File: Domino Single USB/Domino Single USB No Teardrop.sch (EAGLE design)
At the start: 9 parts, among them J1 MH4-1

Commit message: Changed copyright
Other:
- note added: "The Domino Team may make changes to specifications and product"
- note added: "© 2014, The Domino Team All rights reserved."
- note removed: "Michel Stempin may make changes to specifications and product"
- note removed: "© 2014, Michel Stempin All rights reserved."
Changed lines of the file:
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@@
 <text x="302.26" y="12.7" size="0.8128" layer="94">Reference designs are provided "AS IS" and "WITH ALL FAULTS".</text>
 <text x="302.26" y="10.16" size="0.8128" layer="94">regarding this product, including but not limited to, any implied warranties of</text>
-<text x="302.26" y="6.35" size="0.8128" layer="94">Michel Stempin may make changes to specifications and product </text>
+<text x="302.26" y="6.35" size="0.8128" layer="94">The Domino Team may make changes to specifications and product </text>
 <text x="302.26" y="11.43" size="0.8128" layer="94">Global Marine Networks disclaims all other warranties express or implied, </text>
 <text x="302.26" y="8.89" size="0.8128" layer="94">merchantibility or fitness for any particular application.</text>
@@
 <text x="256.54" y="7.62" size="1.778" layer="94" align="center">Domino
 Qi</text>
-<text x="345.44" y="20.32" size="1.27" layer="94">© 2014, Michel Stempin
+<text x="345.44" y="20.32" size="1.27" layer="94">© 2014, The Domino Team
 All rights reserved.</text>
 <text x="379.222" y="5.334" size="1.778" layer="94">&gt;REV</text>

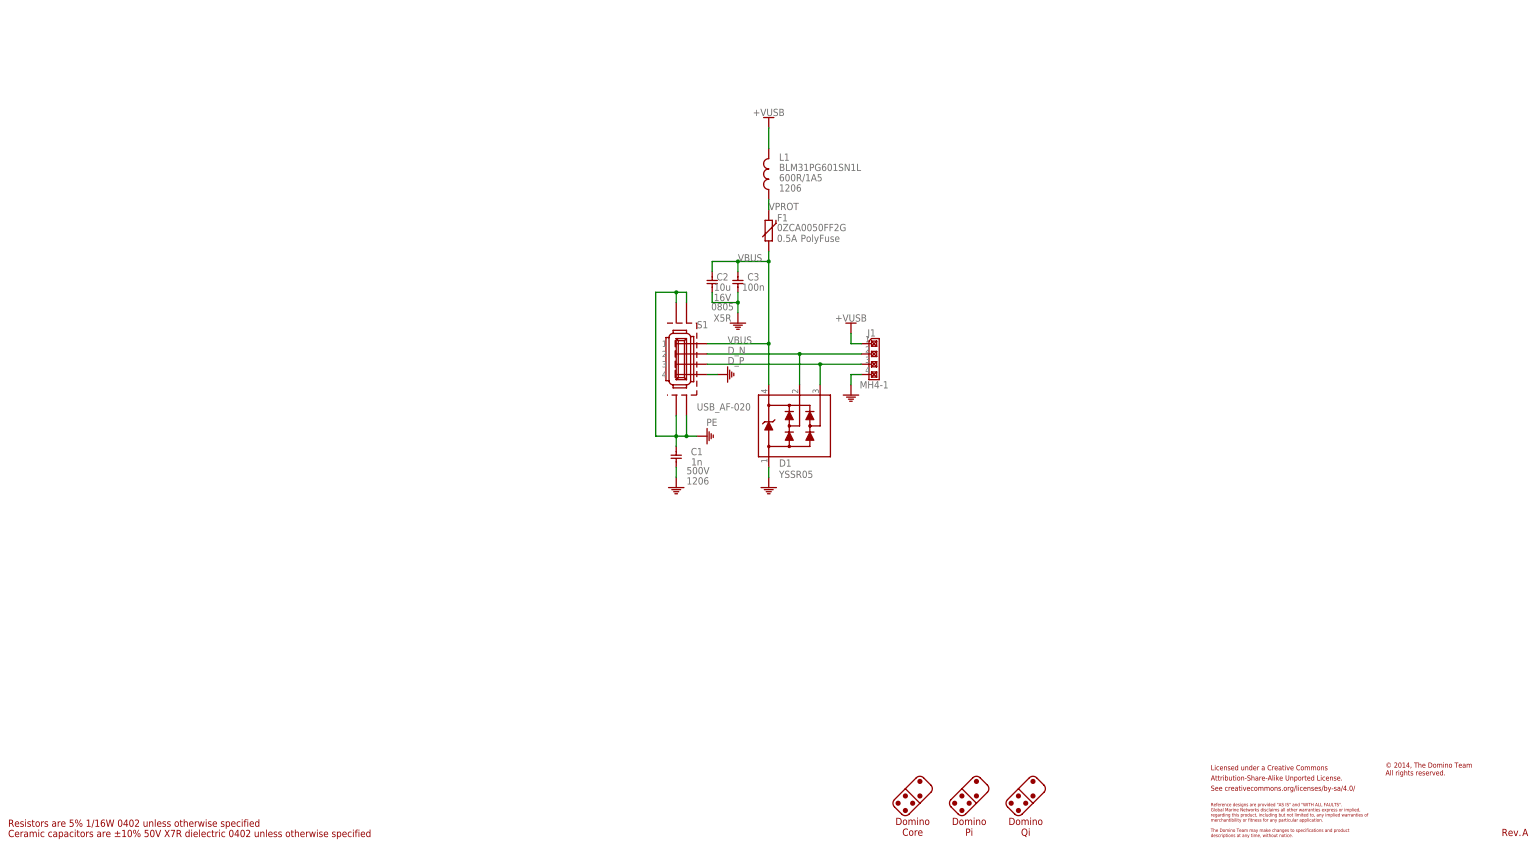
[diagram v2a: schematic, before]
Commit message: Domino Single USB tile Revision B
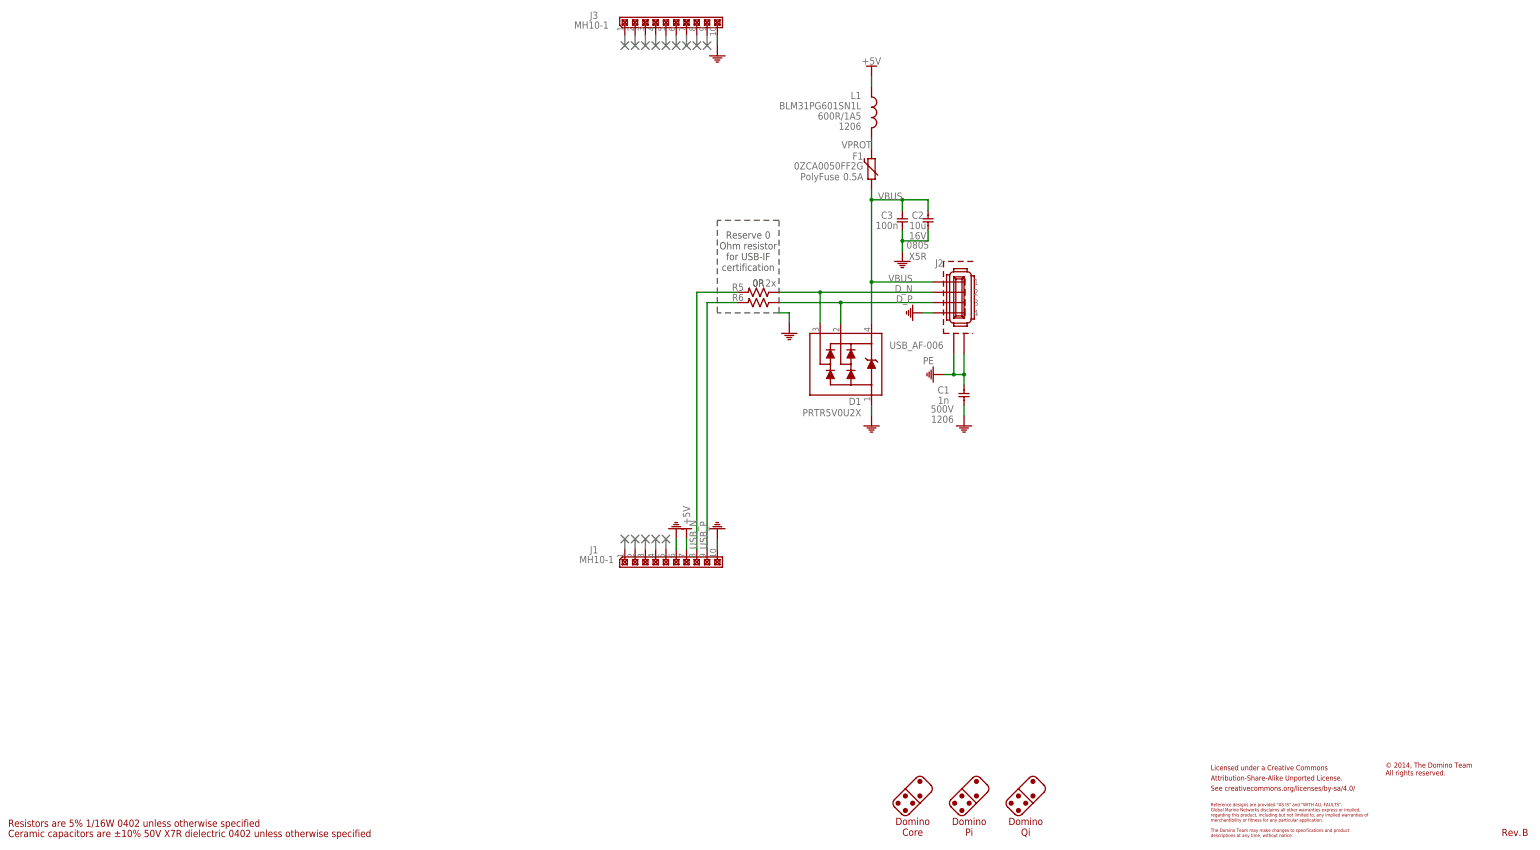
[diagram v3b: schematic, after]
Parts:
- removed S1: USB_AF-020, Domino:USB_AF-020
- added J2: USB_AF-006, Domino:USB_AF-006
- added J3: MH10-1, Domino:MH10-1
- added R5, R6: 0R, Domino:RES_0402
- D1: value YSSR05 -> PRTR5V0U2X; device Domino:YSSR05 -> Domino:PRTR5V0U2X; PARTNO YSSR05 -> PRTR5V0U2X
- J1: value MH4-1 -> MH10-1; device Domino:MH4-1 -> Domino:MH10-1; PARTNO MH4-1-0.1 -> MH10-1-0.1
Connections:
- removed net +VUSB: J1.1, L1.1
- new net +5V: J1.7, L1.1
- new net USB_N: J1.8, R5.2
- new net USB_P: J1.9, R6.2
- net D_N: now also D1.P$3, J2.2, R5.1; no longer D1.P$2, J1.2, S1.2
- net D_P: now also D1.P$2, J2.3, R6.1; no longer D1.P$3, J1.3, S1.3
- net GND: now also J1.10, J1.6, J2.4, J3.10; no longer J1.4, S1.4
- net PE: now also J2.G@1, J2.G@2; no longer S1.G@1, S1.G@2, S1.G@3, S1.G@4
- net VBUS: now also J2.1; no longer S1.1
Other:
- note added: "2x"
- note added: "Reserve 0 Ohm resistor for USB-IF certification"
- moved on the sheet: C1, C2, C3, D1, F1, L1

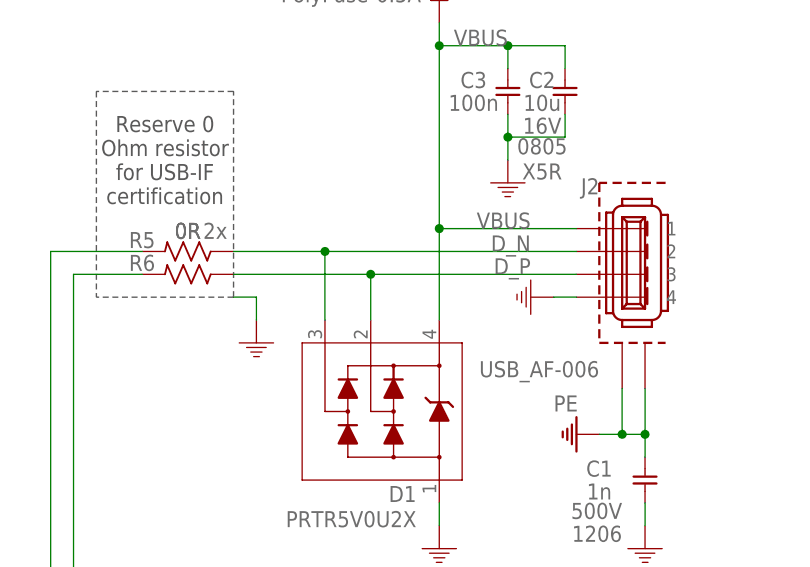
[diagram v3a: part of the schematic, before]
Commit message: Re-routed Single USB tile to remove vias on USB traces
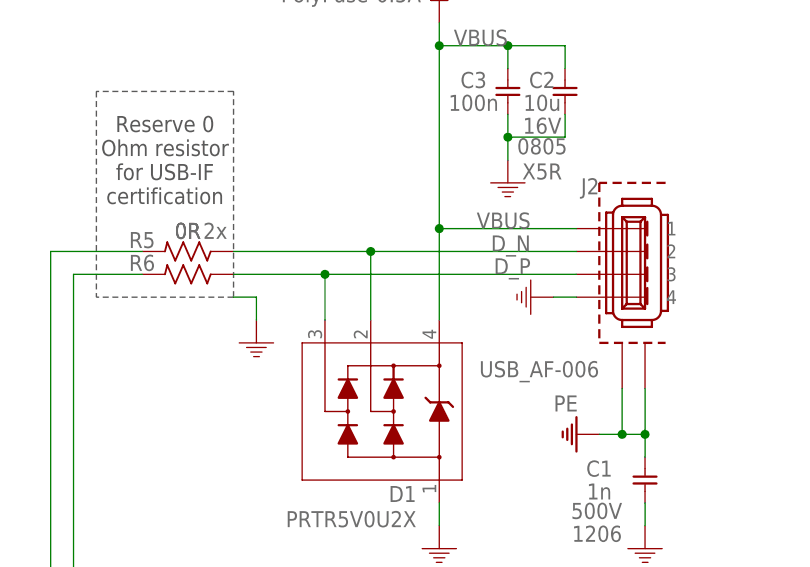
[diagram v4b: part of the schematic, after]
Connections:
- net D_N: now also D1.P$2; no longer D1.P$3
- net D_P: now also D1.P$3; no longer D1.P$2
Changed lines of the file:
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@@
 <net name="D_N" class="1">
 <segment>
-<wire x1="233.68" y1="139.7" x2="205.74" y2="139.7" width="0.1524" layer="91"/>
+<wire x1="233.68" y1="139.7" x2="210.82" y2="139.7" width="0.1524" layer="91"/>
 <label x="228.6" y="139.7" size="1.778" layer="95" rot="MR0"/>
 <pinref part="J2" gate="G$1" pin="2"/>
 <pinref part="R5" gate="G$1" pin="1"/>
-<pinref part="D1" gate="G$1" pin="P$3"/>
-<wire x1="205.74" y1="139.7" x2="195.58" y2="139.7" width="0.1524" layer="91"/>
-<wire x1="205.74" y1="132.08" x2="205.74" y2="139.7" width="0.1524" layer="91"/>
-<junction x="205.74" y="139.7"/>
+<pinref part="D1" gate="G$1" pin="P$2"/>
+<wire x1="210.82" y1="139.7" x2="195.58" y2="139.7" width="0.1524" layer="91"/>
+<wire x1="210.82" y1="132.08" x2="210.82" y2="139.7" width="0.1524" layer="91"/>
+<junction x="210.82" y="139.7"/>
 </segment>
 </net>
 <net name="D_P" class="1">
 <segment>
-<wire x1="195.58" y1="137.16" x2="210.82" y2="137.16" width="0.1524" layer="91"/>
 <label x="228.6" y="137.16" size="1.778" layer="95" rot="MR0"/>
 <pinref part="J2" gate="G$1" pin="3"/>
 <pinref part="R6" gate="G$1" pin="1"/>
-<pinref part="D1" gate="G$1" pin="P$2"/>
-<wire x1="210.82" y1="137.16" x2="233.68" y2="137.16" width="0.1524" layer="91"/>
-<wire x1="210.82" y1="132.08" x2="210.82" y2="137.16" width="0.1524" layer="91"/>
-<junction x="210.82" y="137.16"/>
+<wire x1="195.58" y1="137.16" x2="205.74" y2="137.16" width="0.1524" layer="91"/>
+<pinref part="D1" gate="G$1" pin="P$3"/>
+<wire x1="205.74" y1="137.16" x2="233.68" y2="137.16" width="0.1524" layer="91"/>
+<wire x1="205.74" y1="132.08" x2="205.74" y2="137.16" width="0.1524" layer="91"/>
+<junction x="205.74" y="137.16"/>
 </segment>
 </net>

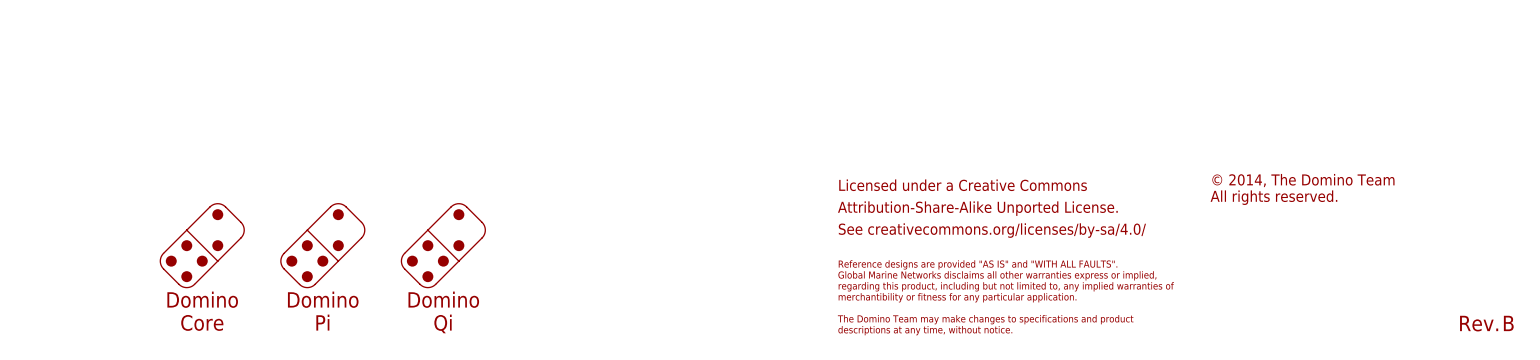
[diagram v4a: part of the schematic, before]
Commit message: Domino Single USB Rev. C: changed Logos
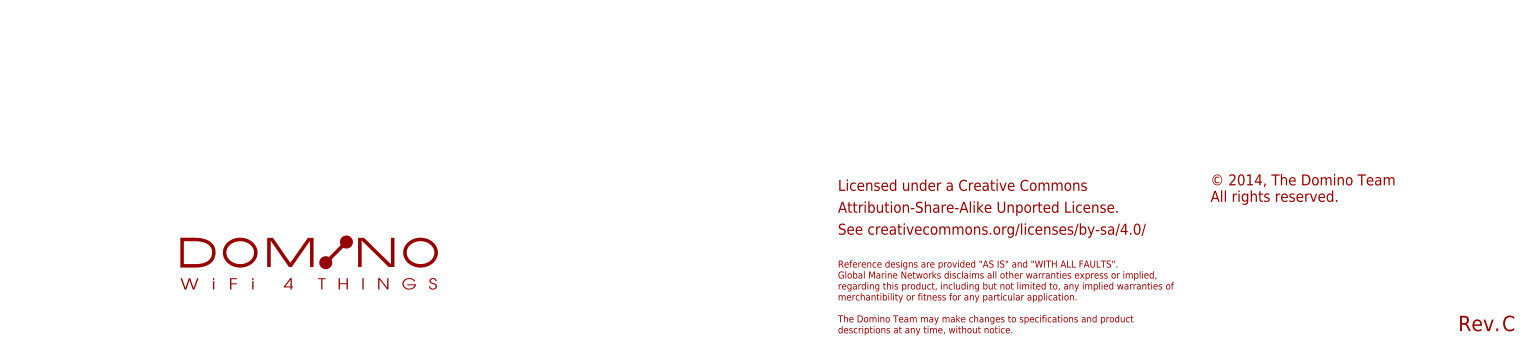
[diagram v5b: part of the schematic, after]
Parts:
- added U$7: DOMINO_LOGO, Domino:DOMINO_LOGO
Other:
- note removed: "Domino Core"
- note removed: "Domino Pi"
- note removed: "Domino Qi"
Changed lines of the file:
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@@
 <layer number="54" name="bGND_GNDA" color="1" fill="9" visible="no" active="no"/>
 <layer number="56" name="wert" color="7" fill="1" visible="no" active="no"/>
+<layer number="90" name="Modules" color="5" fill="1" visible="yes" active="yes"/>
 <layer number="91" name="Nets" color="2" fill="1" visible="yes" active="yes"/>
 <layer number="92" name="Busses" color="1" fill="1" visible="yes" active="yes"/>
@@
 <layer number="143" name="mvRestrict" color="7" fill="1" visible="no" active="no"/>
 <layer number="144" name="Drill_legend" color="7" fill="1" visible="yes" active="yes"/>
+<layer number="145" name="DrillLegend_01-16" color="2" fill="9" visible="yes" active="yes"/>
+<layer number="146" name="DrillLegend_01-20" color="3" fill="9" visible="yes" active="yes"/>
 <layer number="147" name="Measures_X8" color="7" fill="1" visible="yes" active="yes"/>
 <layer number="148" name="mDocument" color="7" fill="1" visible="no" active="no"/>
 <layer number="149" name="mReference" color="7" fill="1" visible="no" active="no"/>
+<layer number="150" name="Pinout" color="7" fill="1" visible="yes" active="yes"/>
 <layer number="151" name="HeatSink" color="7" fill="1" visible="yes" active="yes"/>
 <layer number="152" name="mbDocu" color="7" fill="1" visible="no" active="no"/>
@@
 <attribute name="DATABASE" value="./../Common/BOM/Domino_DB.txt"/>
 <attribute name="DRAWN" value="M.STEMPIN"/>
-<attribute name="REV" value="B"/>
+<attribute name="REV" value="C"/>
 </attributes>
 <variantdefs>
@@
 <part name="PORT13" library="Domino" deviceset="NC" device=""/>
 <part name="PORT14" library="Domino" deviceset="NC" device=""/>
+<part name="U$7" library="Domino" deviceset="DOMINO_LOGO" device=""/>
 </parts>
 <sheets>
@@
 <text x="302.26" y="8.89" size="0.8128" layer="94">merchantibility or fitness for any particular application.</text>
 <text x="302.26" y="5.08" size="0.8128" layer="94">descriptions at any time, without notice.</text>
-<wire x1="238.079875" y1="14.341975" x2="240.77395" y2="17.036053125" width="0.1016" layer="94"/>
-<wire x1="240.77395" y1="17.036053125" x2="243.468028125" y2="19.730128125" width="0.1016" layer="94"/>
-<wire x1="243.468028125" y1="19.730128125" x2="245.264078125" y2="19.730128125" width="0.1016" layer="94" curve="-90"/>
-<wire x1="245.264078125" y1="19.730128125" x2="247.060128125" y2="17.934078125" width="0.1016" layer="94"/>
-<wire x1="247.060128125" y1="17.934078125" x2="247.060128125" y2="16.138028125" width="0.1016" layer="94" curve="-90"/>
-<wire x1="247.060128125" y1="16.138028125" x2="244.366053125" y2="13.44395" width="0.1016" layer="94"/>
-<wire x1="244.366053125" y1="13.44395" x2="241.671975" y2="10.749875" width="0.1016" layer="94"/>
-<wire x1="241.671975" y1="10.749875" x2="239.875925" y2="10.749875" width="0.1016" layer="94" curve="-90"/>
-<wire x1="239.875925" y1="10.749875" x2="238.079875" y2="12.545925" width="0.1016" layer="94"/>
-<wire x1="238.079875" y1="12.545925" x2="238.079875" y2="14.341975" width="0.1016" layer="94" curve="-90"/>
-<wire x1="240.77395" y1="17.036053125" x2="244.366053125" y2="13.44395" width="0.1016" layer="94"/>
-<circle x="238.9779" y="13.44395" radius="0.635" width="0" layer="94"/>
-<circle x="240.77395" y="15.240003125" radius="0.635" width="0" layer="94"/>
-<circle x="240.77395" y="11.6479" radius="0.635" width="0" layer="94"/>
-<circle x="242.57" y="13.44395" radius="0.635" width="0" layer="94"/>
-<circle x="244.366053125" y="15.24" radius="0.635" width="0" layer="94"/>
-<circle x="244.366053125" y="18.832103125" radius="0.635" width="0" layer="94"/>
-<wire x1="224.109875" y1="14.341975" x2="226.80395" y2="17.036053125" width="0.1016" layer="94"/>
-<wire x1="226.80395" y1="17.036053125" x2="229.498028125" y2="19.730128125" width="0.1016" layer="94"/>
-<wire x1="229.498028125" y1="19.730128125" x2="231.294078125" y2="19.730128125" width="0.1016" layer="94" curve="-90"/>
-<wire x1="231.294078125" y1="19.730128125" x2="233.090128125" y2="17.934078125" width="0.1016" layer="94"/>
-<wire x1="233.090128125" y1="17.934078125" x2="233.090128125" y2="16.138028125" width="0.1016" layer="94" curve="-90"/>
-<wire x1="233.090128125" y1="16.138028125" x2="230.396053125" y2="13.44395" width="0.1016" layer="94"/>
-<wire x1="230.396053125" y1="13.44395" x2="227.701975" y2="10.749875" width="0.1016" layer="94"/>
-<wire x1="227.701975" y1="10.749875" x2="225.905925" y2="10.749875" width="0.1016" layer="94" curve="-90"/>
-<wire x1="225.905925" y1="10.749875" x2="224.109875" y2="12.545925" width="0.1016" layer="94"/>
-<wire x1="224.109875" y1="12.545925" x2="224.109875" y2="14.341975" width="0.1016" layer="94" curve="-90"/>
-<wire x1="226.80395" y1="17.036053125" x2="230.396053125" y2="13.44395" width="0.1016" layer="94"/>
-<circle x="225.0079" y="13.44395" radius="0.635" width="0" layer="94"/>
-<circle x="226.80395" y="15.240003125" radius="0.635" width="0" layer="94"/>
-<circle x="226.80395" y="11.6479" radius="0.635" width="0" layer="94"/>
-<circle x="228.6" y="13.44395" radius="0.635" width="0" layer="94"/>
-<circle x="230.396053125" y="15.24" radius="0.635" width="0" layer="94"/>
-<circle x="230.396053125" y="18.832103125" radius="0.635" width="0" layer="94"/>
-<wire x1="252.049875" y1="14.341975" x2="254.74395" y2="17.036053125" width="0.1016" layer="94"/>
-<wire x1="254.74395" y1="17.036053125" x2="257.438028125" y2="19.730128125" width="0.1016" layer="94"/>
-<wire x1="257.438028125" y1="19.730128125" x2="259.234078125" y2="19.730128125" width="0.1016" layer="94" curve="-90"/>
-<wire x1="259.234078125" y1="19.730128125" x2="261.030128125" y2="17.934078125" width="0.1016" layer="94"/>
-<wire x1="261.030128125" y1="17.934078125" x2="261.030128125" y2="16.138028125" width="0.1016" layer="94" curve="-90"/>
-<wire x1="261.030128125" y1="16.138028125" x2="258.336053125" y2="13.44395" width="0.1016" layer="94"/>
-<wire x1="258.336053125" y1="13.44395" x2="255.641975" y2="10.749875" width="0.1016" layer="94"/>
-<wire x1="255.641975" y1="10.749875" x2="253.845925" y2="10.749875" width="0.1016" layer="94" curve="-90"/>
-<wire x1="253.845925" y1="10.749875" x2="252.049875" y2="12.545925" width="0.1016" layer="94"/>
-<wire x1="252.049875" y1="12.545925" x2="252.049875" y2="14.341975" width="0.1016" layer="94" curve="-90"/>
-<wire x1="254.74395" y1="17.036053125" x2="258.336053125" y2="13.44395" width="0.1016" layer="94"/>
-<circle x="252.9479" y="13.44395" radius="0.635" width="0" layer="94"/>
-<circle x="254.74395" y="15.240003125" radius="0.635" width="0" layer="94"/>
-<circle x="254.74395" y="11.6479" radius="0.635" width="0" layer="94"/>
-<circle x="256.54" y="13.44395" radius="0.635" width="0" layer="94"/>
-<circle x="258.336053125" y="15.24" radius="0.635" width="0" layer="94"/>
-<circle x="258.336053125" y="18.832103125" radius="0.635" width="0" layer="94"/>
-<text x="228.6" y="7.62" size="1.778" layer="94" align="center">Domino
-Core</text>
-<text x="242.57" y="7.62" size="1.778" layer="94" align="center">Domino
-Pi</text>
-<text x="256.54" y="7.62" size="1.778" layer="94" align="center">Domino
-Qi</text>
 <text x="345.44" y="20.32" size="1.27" layer="94">© 2014, The Domino Team
 All rights reserved.</text>
@@
 <instance part="PORT13" gate="G$1" x="165.1" y="78.74" rot="R270"/>
 <instance part="PORT14" gate="G$1" x="167.64" y="78.74" rot="R270"/>
+<instance part="U$7" gate="G$1" x="226.06" y="12.7"/>
 </instances>
 <busses>
